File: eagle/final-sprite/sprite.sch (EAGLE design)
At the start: 43 parts, among them P1 SPRITE_PIN, P2 SPRITE_PIN, U1 CC430F5137, U2 DRV8833CRTER, X1 TCXO_7Z

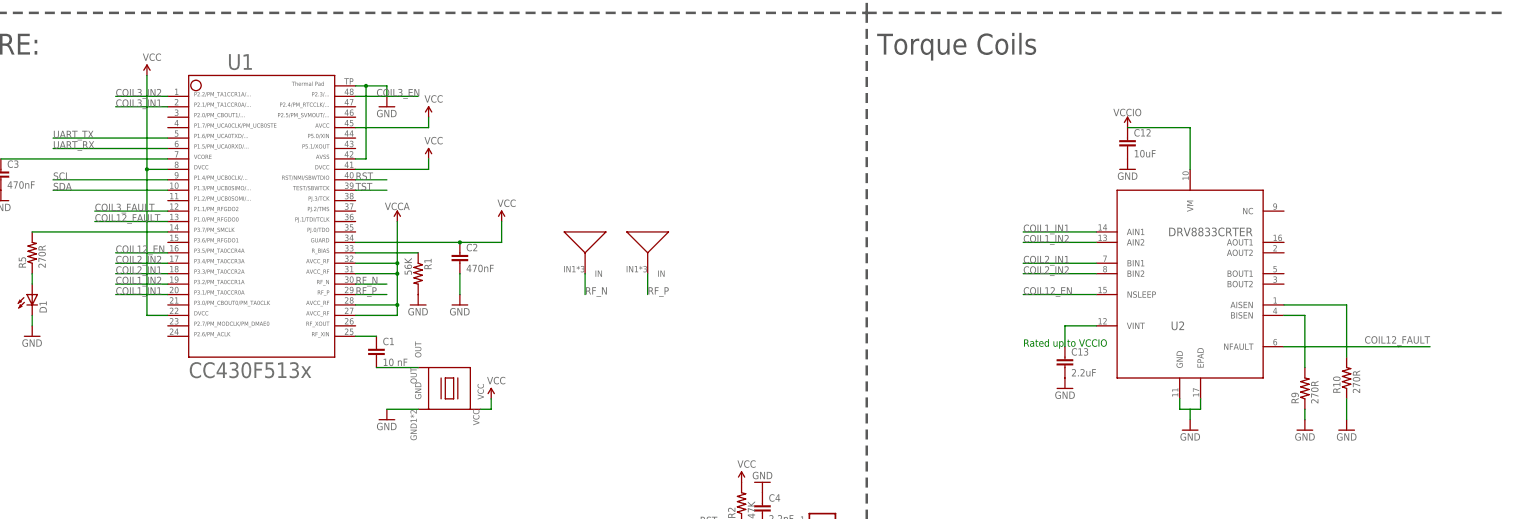
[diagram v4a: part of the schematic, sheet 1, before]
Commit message: Complete one driver
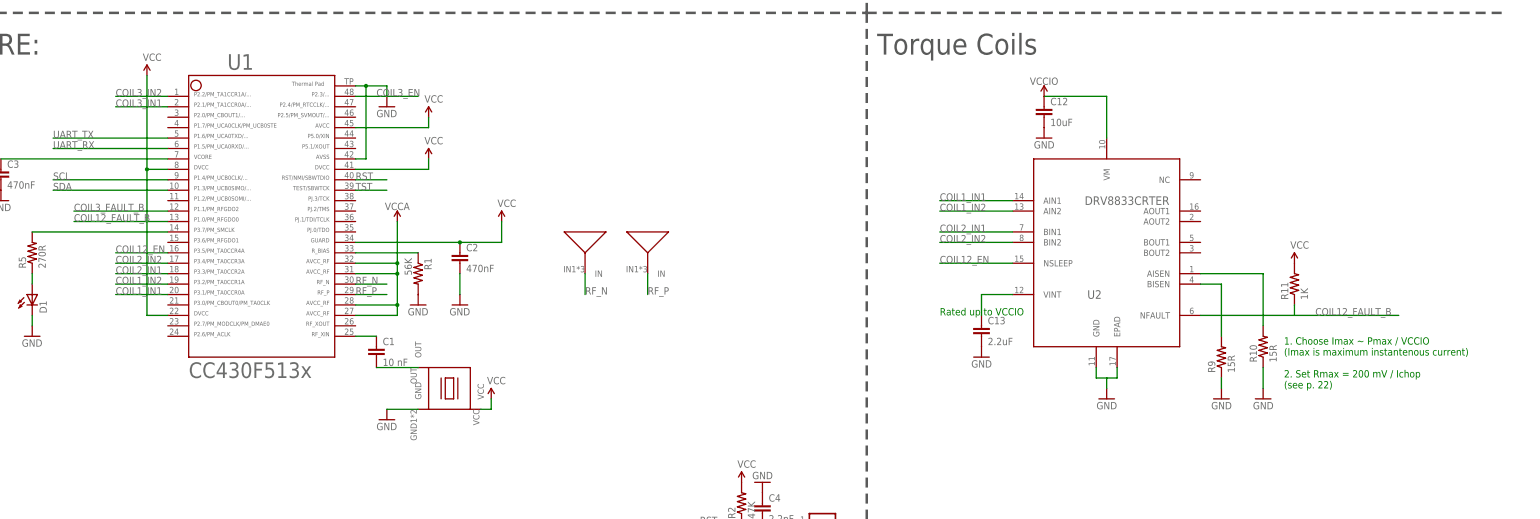
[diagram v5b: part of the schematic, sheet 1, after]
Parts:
- added R11: 1K, SparkFun:RESISTOR0603-RES
- R10, R9: value 270R -> 15R
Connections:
- net COIL3_FAULT renamed COIL3_FAULT_B
- removed net COIL12_FAULT: U1.13, U2.NFAULT
- new net COIL12_FAULT_B: R11.1, U1.13, U2.NFAULT
- net VCC: now also R11.2
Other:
- note added: "1. Choose Imax ~ Pmax / VCCIO (Imax is maximum instantenous current) 2. Set Rmax = 200 mV / Ichop (see p. 22)"
- moved on the sheet: C12, C13, R10, R9, U2

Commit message: Giving Kevin more space
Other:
- note removed: "Accelerometer, Magnetometer, Gyroscope"
- moved on the sheet: C4, JP2, JP3, R2
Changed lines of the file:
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@@
 <?xml version="1.0" encoding="utf-8"?>
 <!DOCTYPE eagle SYSTEM "eagle.dtd">
-<eagle version="9.0.0">
+<eagle version="9.0.1">
 <drawing>
 <settings>
@@
 <sheet>
 <plain>
-<wire x1="-73.66" y1="-167.64" x2="149.86" y2="-167.64" width="0.6096" layer="97" style="longdash"/>
+<wire x1="-73.66" y1="-167.64" x2="66.04" y2="-167.64" width="0.6096" layer="97" style="longdash"/>
+<wire x1="66.04" y1="-167.64" x2="149.86" y2="-167.64" width="0.6096" layer="97" style="longdash"/>
 <wire x1="149.86" y1="-167.64" x2="149.86" y2="-66.04" width="0.6096" layer="97" style="longdash"/>
-<wire x1="149.86" y1="-167.64" x2="149.86" y2="-317.5" width="0.6096" layer="97" style="longdash"/>
-<text x="-17.78" y="-73.66" size="2.54" layer="97">Accelerometer, Magnetometer, Gyroscope</text>
 <text x="93.98" y="-73.66" size="2.54" layer="97">Sun Sensors</text>
 <text x="-71.12" y="-73.66" size="5.08" layer="97">Sensing:</text>
@@
 2. Set Rmax = 200 mV / Ichop
 (see p. 22)</text>
+<wire x1="66.04" y1="-314.96" x2="66.04" y2="-167.64" width="0.6096" layer="97" style="longdash"/>
 </plain>
 <instances>
@@
 <instance part="GND16" gate="1" x="292.1" y="-86.36"/>
 <instance part="P+4" gate="1" x="292.1" y="-73.66"/>
-<instance part="JP3" gate="G$1" x="139.7" y="-302.26" rot="R180"/>
+<instance part="JP3" gate="G$1" x="-33.02" y="-304.8" rot="R180"/>
 <instance part="P1" gate="G$1" x="279.4" y="-73.66"/>
 <instance part="P2" gate="G$1" x="279.4" y="-83.82"/>
@@
 <instance part="GND8" gate="1" x="33.02" y="-266.7"/>
 <instance part="P+2" gate="1" x="43.18" y="-193.04"/>
-<instance part="JP2" gate="G$1" x="139.7" y="-292.1" rot="R180"/>
-<instance part="ANT-N" gate="G$1" x="81.28" y="-226.06"/>
-<instance part="ANT-P" gate="G$1" x="96.52" y="-226.06"/>
-<instance part="R2" gate="G$1" x="119.38" y="-287.02" rot="R90"/>
-<instance part="C4" gate="G$1" x="124.46" y="-289.56"/>
-<instance part="GND2" gate="1" x="124.46" y="-281.94" rot="R180"/>
-<instance part="P+5" gate="1" x="119.38" y="-281.94"/>
+<instance part="JP2" gate="G$1" x="-33.02" y="-294.64" rot="R180"/>
+<instance part="ANT-N" gate="G$1" x="-15.24" y="-297.18"/>
+<instance part="ANT-P" gate="G$1" x="0" y="-297.18"/>
+<instance part="R2" gate="G$1" x="-53.34" y="-289.56" rot="R90"/>
+<instance part="C4" gate="G$1" x="-48.26" y="-292.1"/>
+<instance part="GND2" gate="1" x="-48.26" y="-284.48" rot="R180"/>
+<instance part="P+5" gate="1" x="-53.34" y="-284.48"/>
 <instance part="P+8" gate="1" x="43.18" y="-203.2"/>
 <instance part="P+9" gate="1" x="60.96" y="-218.44"/>
@@
 <segment>
 <pinref part="JP3" gate="G$1" pin="2"/>
-<wire x1="132.08" y1="-304.8" x2="129.54" y2="-304.8" width="0.1524" layer="91"/>
-<label x="129.54" y="-304.8" size="1.778" layer="95" rot="MR0"/>
+<wire x1="-40.64" y1="-307.34" x2="-43.18" y2="-307.34" width="0.1524" layer="91"/>
+<label x="-43.18" y="-307.34" size="1.778" layer="95" rot="MR0"/>
 </segment>
 <segment>
@@
 <segment>
 <pinref part="JP3" gate="G$1" pin="1"/>
-<wire x1="132.08" y1="-302.26" x2="129.54" y2="-302.26" width="0.1524" layer="91"/>
-<label x="129.54" y="-302.26" size="1.778" layer="95" rot="MR0"/>
+<wire x1="-40.64" y1="-304.8" x2="-43.18" y2="-304.8" width="0.1524" layer="91"/>
+<label x="-43.18" y="-304.8" size="1.778" layer="95" rot="MR0"/>
 </segment>
 <segment>
@@
 <pinref part="JP2" gate="G$1" pin="1"/>
 <pinref part="C4" gate="G$1" pin="2"/>
-<wire x1="124.46" y1="-292.1" x2="132.08" y2="-292.1" width="0.1524" layer="91"/>
+<wire x1="-48.26" y1="-294.64" x2="-40.64" y2="-294.64" width="0.1524" layer="91"/>
 <pinref part="R2" gate="G$1" pin="1"/>
-<wire x1="124.46" y1="-292.1" x2="119.38" y2="-292.1" width="0.1524" layer="91"/>
-<junction x="124.46" y="-292.1"/>
-<wire x1="119.38" y1="-292.1" x2="109.22" y2="-292.1" width="0.1524" layer="91"/>
-<junction x="119.38" y="-292.1"/>
-<label x="109.22" y="-292.1" size="1.778" layer="95"/>
+<wire x1="-48.26" y1="-294.64" x2="-53.34" y2="-294.64" width="0.1524" layer="91"/>
+<junction x="-48.26" y="-294.64"/>
+<wire x1="-53.34" y1="-294.64" x2="-63.5" y2="-294.64" width="0.1524" layer="91"/>
+<junction x="-53.34" y="-294.64"/>
+<label x="-63.5" y="-294.64" size="1.778" layer="95"/>
 </segment>
 </net>
@@
 <segment>
 <pinref part="JP2" gate="G$1" pin="2"/>
-<wire x1="132.08" y1="-294.64" x2="109.22" y2="-294.64" width="0.1524" layer="91"/>
-<label x="109.22" y="-294.64" size="1.778" layer="95"/>
+<wire x1="-40.64" y1="-297.18" x2="-63.5" y2="-297.18" width="0.1524" layer="91"/>
+<label x="-63.5" y="-297.18" size="1.778" layer="95"/>
 </segment>
 </net>
@@
 <segment>
 <pinref part="ANT-N" gate="G$1" pin="IN"/>
-<wire x1="81.28" y1="-231.14" x2="81.28" y2="-236.22" width="0.1524" layer="91"/>
-<label x="81.28" y="-236.22" size="1.778" layer="95"/>
+<wire x1="-15.24" y1="-302.26" x2="-15.24" y2="-307.34" width="0.1524" layer="91"/>
+<label x="-15.24" y="-307.34" size="1.778" layer="95"/>
 </segment>
 </net>
@@
 <segment>
 <pinref part="ANT-P" gate="G$1" pin="IN"/>
-<wire x1="96.52" y1="-236.22" x2="96.52" y2="-231.14" width="0.1524" layer="91"/>
-<label x="96.52" y="-236.22" size="1.778" layer="95"/>
-</segment>
-</net>
+<wire x1="0" y1="-307.34" x2="0" y2="-302.26" width="0.1524" layer="91"/>
+<label x="0" y="-307.34" size="1.778" layer="95"/>
+</segment>
+</net>

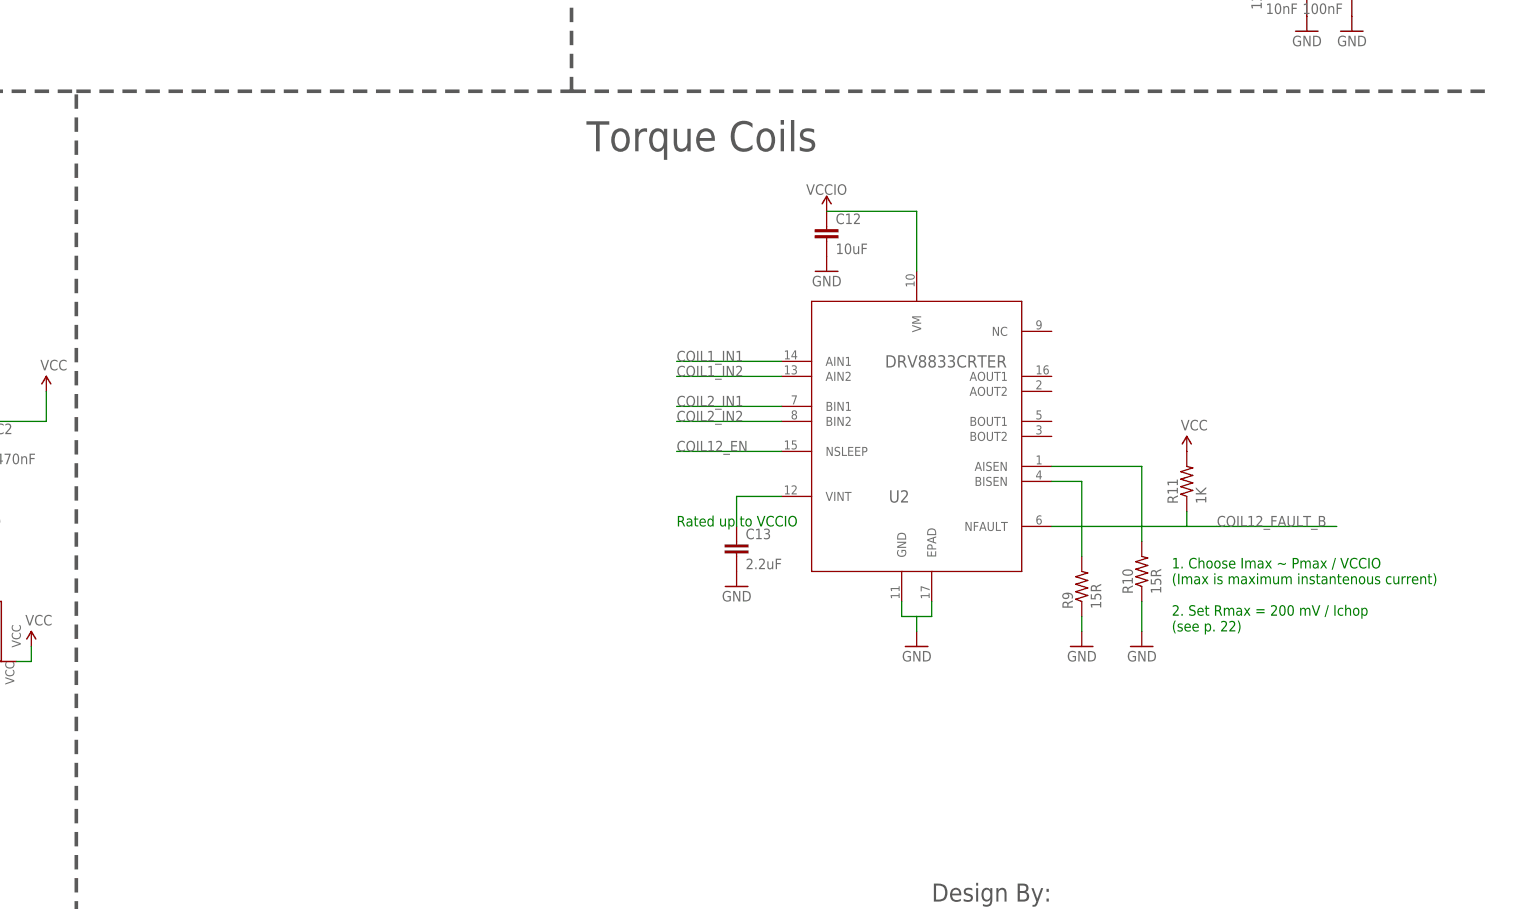
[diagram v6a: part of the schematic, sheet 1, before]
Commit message: Add second driver
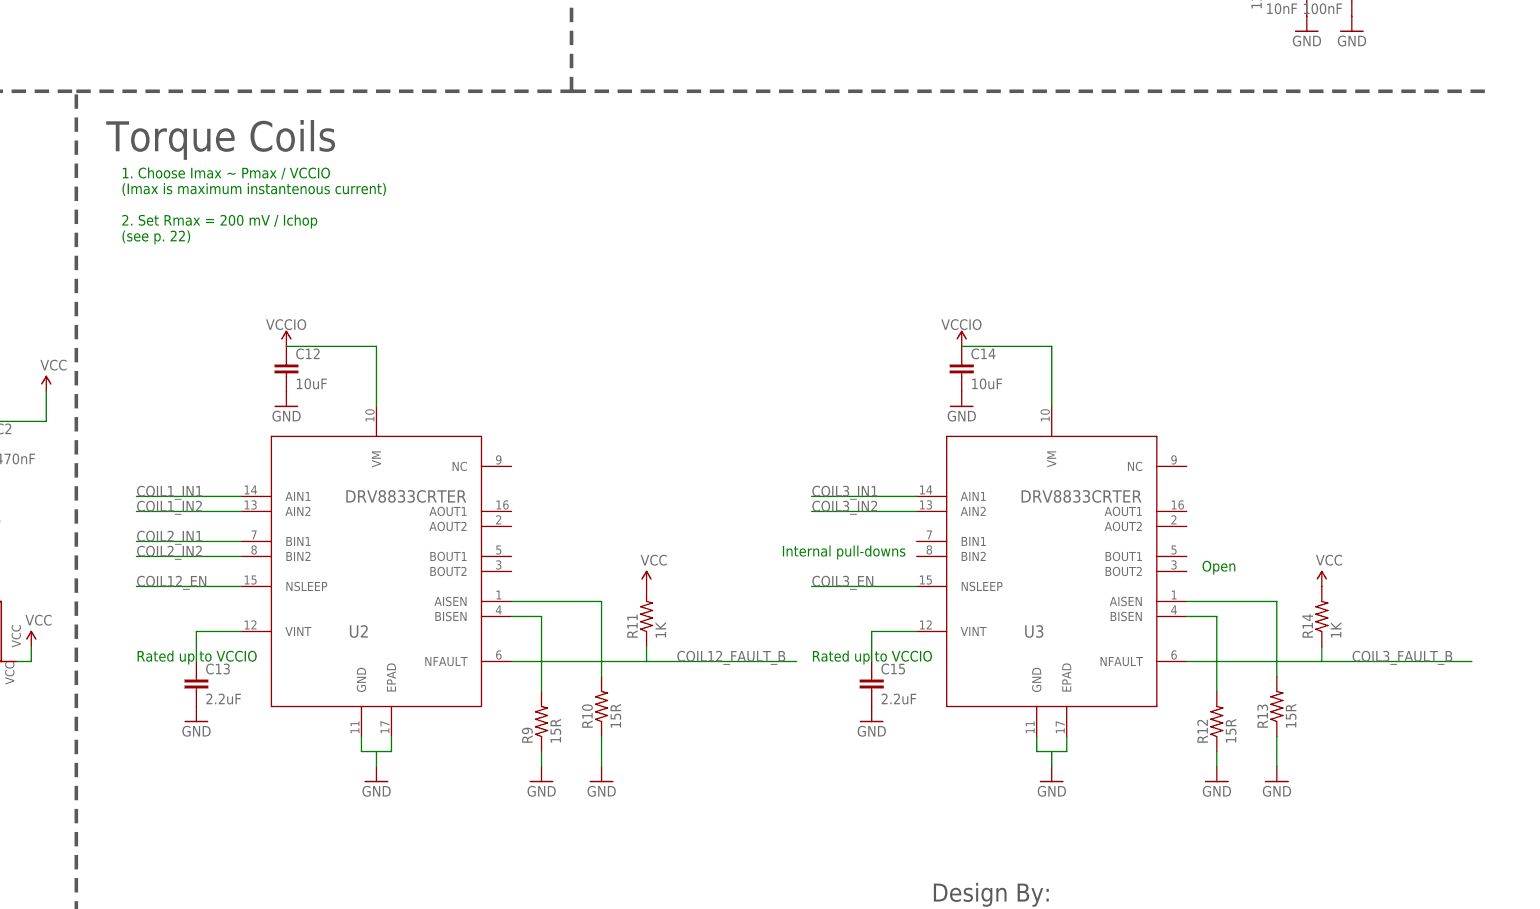
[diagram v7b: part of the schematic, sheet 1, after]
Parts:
- added C14: 10uF, SparkFun:CAP0603-CAP
- added C15: 2.2uF, SparkFun:CAP0603-CAP
- added R12, R13: 15R, SparkFun:RESISTOR0603-RES
- added R14: 1K, SparkFun:RESISTOR0603-RES
- added U3: DRV8833CRTER, STAC:DRV8833CRTER
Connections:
- new net N$13: C15.1, U3.VINT
- new net N$14: R12.2, U3.BISEN
- new net N$15: R13.2, U3.AISEN
- net COIL3_EN: now also U3.NSLEEP
- net COIL3_FAULT_B: now also R14.1, U3.NFAULT
- net COIL3_IN1: now also U3.AIN1
- net COIL3_IN2: now also U3.AIN2
- net GND: now also C14.2, C15.2, R12.1, R13.1, U3.EPAD, U3.GND
- net VCC: now also R14.2
- net VCCIO: now also C14.1, U3.VM
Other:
- note added: "Internal pull-downs"
- note added: "Open"
- moved on the sheet: C12, C13, R10, R11, R9, U2

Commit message: adding power stuff
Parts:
- added C16, C17: (no value), resistor:C-EUC0402
- added R15, R16, R17, R18, R19, R20, R21, R22, R23: (no value), resistor:R-US_R0402
- added U$5: LPS4018-223M, STAC:LPS4018-223M
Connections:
- new net DSW: U$4.DIS_SW, U1.24
- new net N$18: R16.2, R17.1, U$4.MPPT
- new net N$20: R15.2, U$4.MINOP
- new net N$21: C16.1, U$4.CBP
- new net N$22: U$4.SW, U$5.P$2
- new net REF: R18.2, R20.2, U$4.REF
- new net REG_D0: U$4.REG_D0, U1.3
- new net REG_D1: U$4.REG_D1, U1.4
- new net SETHYS: R21.1, R22.2, U$4.SETHYST
- new net SETPG: R20.1, R21.2, U$4.SETPG
- new net SETSD: R19.2, R23.1, U$4.SETSD
- new net TERM: R18.1, R23.2, U$4.TERM
- new net VID: U$4.VID, U1.23
- net GND: now also C16.2, C17.2, R15.1, R16.1, R19.1, R22.1, U$4.SETBK
- net PGOOD: now also U1.46
- net REGGOOD: now also U1.47
- net VCCINT: now also C17.1, R17.2, U$4.VIN, U$5.P$1
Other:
- moved on the sheet: S1, S2, S3, S4, U$4
